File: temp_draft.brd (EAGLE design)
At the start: 76.7 x 34.5 mm, 39 parts, among them IC1 NCS21911SN2T1G, IC2 NCS21911SN2T1G, IC3 NCS21911SN2T1G, IC4 NCS21911SN2T1G

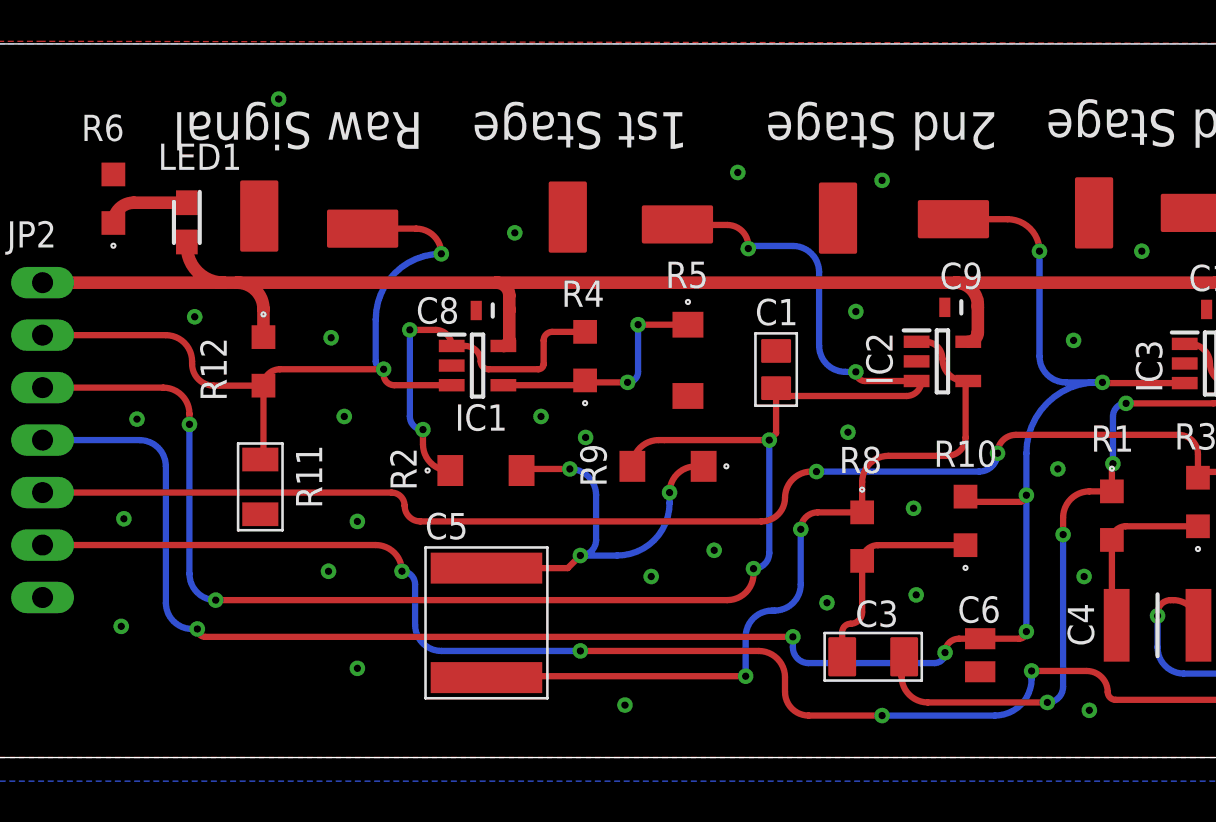
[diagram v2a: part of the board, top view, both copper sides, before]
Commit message: changed vias to GND vias
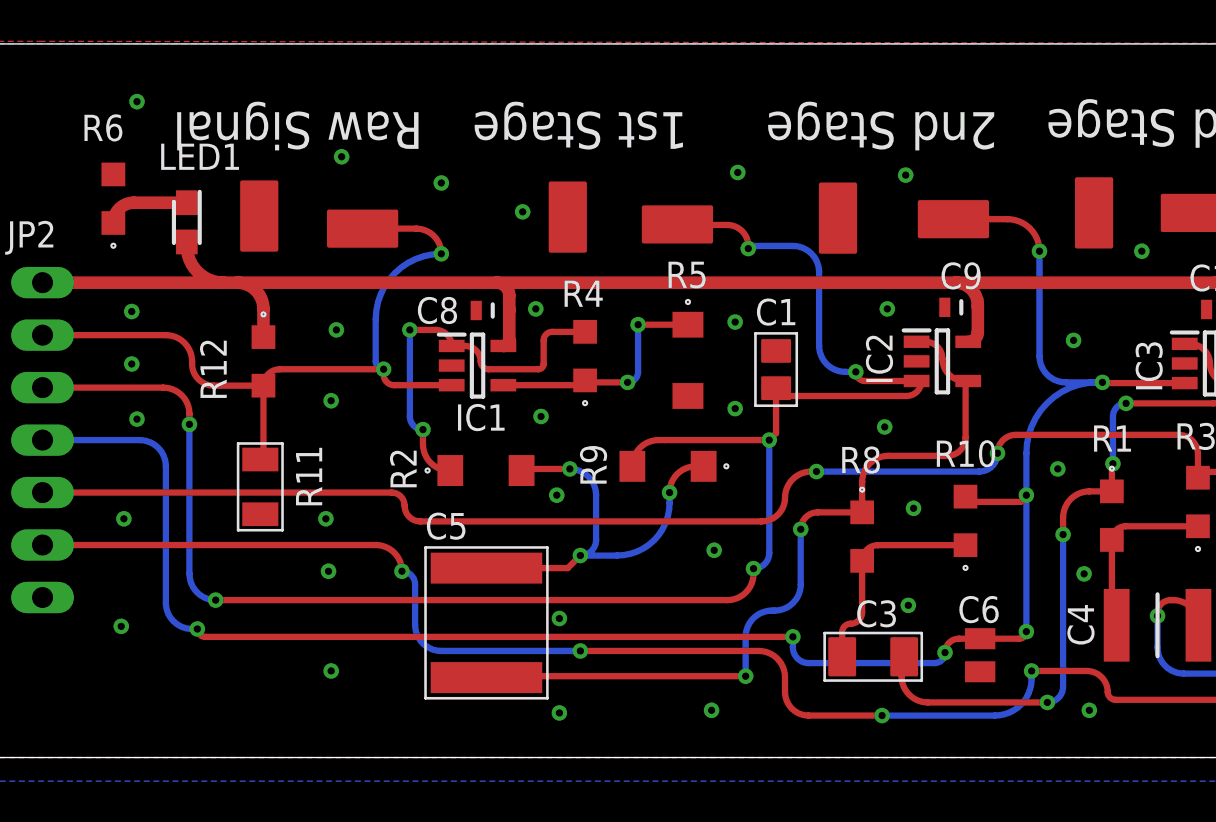
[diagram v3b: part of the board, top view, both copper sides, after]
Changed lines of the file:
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@@
 <drawing>
 <settings>
-<setting alwaysvectorfont="yes"/>
+<setting alwaysvectorfont="no"/>
 <setting verticaltext="up"/>
 </settings>
@@
 <vertex x="76.454" y="34.544"/>
 </polygon>
-<via x="13.97" y="31.877" extent="1-16" drill="0.35"/>
+<via x="7.112" y="31.75" extent="1-16" drill="0.35"/>
 <contactref element="R6" pad="2"/>
-<wire x1="67.272" y1="21.463" x2="65.2018" y2="26.4922" width="0" layer="19" extent="1-1"/>
-<wire x1="66.0854" y1="18.8976" x2="67.272" y2="21.463" width="0" layer="19" extent="1-1"/>
-<wire x1="58.89" y1="21.6916" x2="66.0854" y2="18.8976" width="0" layer="19" extent="1-1"/>
-<wire x1="57.8304" y1="19.0754" x2="58.89" y2="21.6916" width="0" layer="19" extent="1-1"/>
-<wire x1="53.4416" y1="26.3652" x2="58.89" y2="21.6916" width="0" layer="19" extent="1-1"/>
-<wire x1="65.7352" y1="11.0716" x2="66.0854" y2="18.8976" width="0" layer="19" extent="1-1"/>
-<wire x1="62.23" y1="11.066" x2="65.7352" y2="11.0716" width="0" layer="19" extent="1-1"/>
-<wire x1="46.2154" y1="21.7932" x2="53.4416" y2="26.3652" width="0" layer="19" extent="1-1"/>
-<wire x1="44.851" y1="19.177" x2="46.2154" y2="21.7932" width="0" layer="19" extent="1-1"/>
-<wire x1="41.0464" y1="26.1112" x2="46.2154" y2="21.7932" width="0" layer="19" extent="1-1"/>
-<wire x1="38.0492" y1="19.6816" x2="44.851" y2="19.177" width="0" layer="19" extent="1-1"/>
-<wire x1="33.782" y1="17.5028" x2="38.0492" y2="19.6816" width="0" layer="19" extent="1-1"/>
-<wire x1="27.9654" y1="26.162" x2="33.782" y2="17.5028" width="0" layer="19" extent="1-1"/>
-<wire x1="23.5332" y1="21.6408" x2="27.9654" y2="26.162" width="0" layer="19" extent="1-1"/>
-<wire x1="22.3466" y1="18.9738" x2="23.5332" y2="21.6408" width="0" layer="19" extent="1-1"/>
-<wire x1="13.0302" y1="26.2128" x2="23.5332" y2="21.6408" width="0" layer="19" extent="1-1"/>
-<wire x1="13.97" y1="31.877" x2="13.0302" y2="26.2128" width="0" layer="19" extent="1-1"/>
-<wire x1="13.081" y1="11.7772" x2="22.3466" y2="18.9738" width="0" layer="19" extent="1-1"/>
-<wire x1="2.54" y1="7.747" x2="13.081" y2="11.7772" width="0" layer="19" extent="1-1"/>
-<wire x1="5.969" y1="28.226" x2="2.54" y2="7.747" width="0" layer="19" extent="1-1"/>
-<wire x1="47.9298" y1="4.153" x2="44.851" y2="19.177" width="0" layer="19" extent="1-1"/>
+<via x="16.764" y="20.701" extent="1-16" drill="0.35"/>
+<via x="21.844" y="27.813" extent="1-16" drill="0.35"/>
+<via x="17.018" y="29.083" extent="1-16" drill="0.35"/>
+<via x="16.256" y="11.557" extent="1-16" drill="0.35"/>
+<via x="16.383" y="9.017" extent="1-16" drill="0.35"/>
+<via x="6.35" y="6.35" extent="1-16" drill="0.35"/>
+<via x="36.195" y="28.321" extent="1-16" drill="0.35"/>
+<via x="74.168" y="26.289" extent="1-16" drill="0.35"/>
+<via x="74.041" y="21.209" extent="1-16" drill="0.35"/>
+<via x="73.406" y="15.494" extent="1-16" drill="0.35"/>
+<via x="71.628" y="10.541" extent="1-16" drill="0.35"/>
+<via x="71.12" y="4.826" extent="1-16" drill="0.35"/>
+<via x="53.213" y="2.286" extent="1-16" drill="0.35"/>
+<via x="34.925" y="2.286" extent="1-16" drill="0.35"/>
+<via x="27.559" y="2.159" extent="1-16" drill="0.35"/>
+<via x="16.51" y="4.191" extent="1-16" drill="0.35"/>
+<via x="43.434" y="21.717" extent="1-16" drill="0.35"/>
+<via x="36.068" y="21.082" extent="1-16" drill="0.35"/>
+<via x="62.865" y="27.051" extent="1-16" drill="0.35"/>
+<via x="64.643" y="21.463" extent="1-16" drill="0.35"/>
+<via x="65.024" y="4.572" extent="1-16" drill="0.35"/>
+<via x="35.052" y="10.033" extent="1-16" drill="0.35"/>
+<via x="6.858" y="19.05" extent="1-16" drill="0.35"/>
+<via x="6.858" y="21.59" extent="1-16" drill="0.35"/>
+<via x="16.51" y="17.272" extent="1-16" drill="0.35"/>
+<via x="7.112" y="16.383" extent="1-16" drill="0.35"/>
+<via x="6.477" y="11.557" extent="1-16" drill="0.35"/>
+<via x="27.559" y="6.731" extent="1-16" drill="0.35"/>
+<via x="36.068" y="16.891" extent="1-16" drill="0.35"/>
+<via x="25.781" y="26.416" extent="1-16" drill="0.35"/>
+<via x="44.323" y="28.194" extent="1-16" drill="0.35"/>
+<via x="55.753" y="24.511" extent="1-16" drill="0.35"/>
+<via x="52.451" y="20.193" extent="1-16" drill="0.35"/>
+<via x="51.689" y="13.97" extent="1-16" drill="0.35"/>
+<via x="52.959" y="8.89" extent="1-16" drill="0.35"/>
+<via x="64.008" y="16.129" extent="1-16" drill="0.35"/>
+<via x="26.416" y="21.717" extent="1-16" drill="0.35"/>
+<via x="26.67" y="16.51" extent="1-16" drill="0.35"/>
+<via x="27.432" y="12.7" extent="1-16" drill="0.35"/>
+<via x="44.45" y="7.366" extent="1-16" drill="0.35"/>
+<via x="44.704" y="12.065" extent="1-16" drill="0.35"/>
+<via x="43.307" y="16.002" extent="1-16" drill="0.35"/>
+<via x="64.008" y="9.525" extent="1-16" drill="0.35"/>
 </signal>
 <signal name="N$1">
@@
 <wire x1="25.1332" y1="22.3648" x2="24.511" y2="22.987" width="0.6096" layer="1" curve="90"/>
 </signal>
-<signal name="GND1">
-<via x="9.906" y="21.336" extent="1-16" drill="0.35"/>
-</signal>
-<signal name="GND2">
-<via x="6.35" y="6.35" extent="1-16" drill="0.35"/>
-</signal>
-<signal name="GND3">
-<via x="16.51" y="20.32" extent="1-16" drill="0.35"/>
-</signal>
-<signal name="GND4">
-<via x="17.78" y="11.43" extent="1-16" drill="0.35"/>
-</signal>
-<signal name="GND5">
-<via x="17.78" y="4.318" extent="1-16" drill="0.35"/>
-</signal>
-<signal name="GND6">
-<via x="25.4" y="25.4" extent="1-16" drill="0.35"/>
-</signal>
-<signal name="GND7">
-<via x="26.67" y="16.51" extent="1-16" drill="0.35"/>
-</signal>
-<signal name="GND8">
-<via x="32.004" y="8.763" extent="1-16" drill="0.35"/>
-</signal>
-<signal name="GND9">
-<via x="30.734" y="2.54" extent="1-16" drill="0.35"/>
-</signal>
-<signal name="GND10">
-<via x="43.18" y="27.94" extent="1-16" drill="0.35"/>
-</signal>
-<signal name="GND11">
-<via x="41.91" y="21.59" extent="1-16" drill="0.35"/>
-</signal>
-<signal name="GND12">
-<via x="41.529" y="15.748" extent="1-16" drill="0.35"/>
-</signal>
-<signal name="GND13">
-<via x="40.513" y="7.493" extent="1-16" drill="0.35"/>
-</signal>
-<signal name="GND14">
-<via x="52.451" y="20.193" extent="1-16" drill="0.35"/>
-</signal>
-<signal name="GND15">
-<via x="51.689" y="13.97" extent="1-16" drill="0.35"/>
-</signal>
-<signal name="GND16">
-<via x="52.959" y="8.763" extent="1-16" drill="0.35"/>
-</signal>
-<signal name="GND17">
-<via x="62.865" y="27.051" extent="1-16" drill="0.35"/>
-</signal>
-<signal name="GND18">
-<via x="64.643" y="21.463" extent="1-16" drill="0.35"/>
-</signal>
-<signal name="GND19">
-<via x="64.008" y="16.129" extent="1-16" drill="0.35"/>
-</signal>
-<signal name="GND20">
-<via x="65.024" y="4.572" extent="1-16" drill="0.35"/>
-</signal>
-<signal name="GND21">
-<via x="7.112" y="16.383" extent="1-16" drill="0.35"/>
-</signal>
-<signal name="GND22">
-<via x="64.008" y="9.525" extent="1-16" drill="0.35"/>
-</signal>
-<signal name="N$2">
-<via x="6.477" y="11.557" extent="1-16" drill="0.35"/>
-</signal>
-<signal name="N$3">
-<via x="17.145" y="16.51" extent="1-16" drill="0.35"/>
-</signal>
-<signal name="N$4">
-<via x="16.383" y="9.017" extent="1-16" drill="0.35"/>
-</signal>
-<signal name="N$8">
-<via x="28.829" y="15.494" extent="1-16" drill="0.35"/>
-</signal>
-<signal name="N$9">
-<via x="35.052" y="10.033" extent="1-16" drill="0.35"/>
-</signal>
-<signal name="N$10">
-<via x="44.831" y="7.874" extent="1-16" drill="0.35"/>
-</signal>
-<signal name="N$11">
-<via x="44.704" y="12.065" extent="1-16" drill="0.35"/>
-</signal>
-<signal name="N$12">
-<via x="55.753" y="24.511" extent="1-16" drill="0.35"/>
-</signal>
-<signal name="N$13">
-<via x="53.213" y="2.286" extent="1-16" drill="0.35"/>
-</signal>
-<signal name="N$14">
-<via x="74.168" y="26.289" extent="1-16" drill="0.35"/>
-</signal>
-<signal name="N$15">
-<via x="74.041" y="21.209" extent="1-16" drill="0.35"/>
-</signal>
-<signal name="N$16">
-<via x="73.406" y="15.494" extent="1-16" drill="0.35"/>
-</signal>
-<signal name="N$17">
-<via x="71.628" y="10.541" extent="1-16" drill="0.35"/>
-</signal>
-<signal name="N$18">
-<via x="71.12" y="4.826" extent="1-16" drill="0.35"/>
-</signal>
-<signal name="N$19">
-<via x="36.195" y="28.321" extent="1-16" drill="0.35"/>
-</signal>
 <signal name="N$20">

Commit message: updated labels
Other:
- board size 76.7 x 34.5 mm -> 82.2 x 34.5 mm
- board text added: "BAJA SAE ELECTRICALS DESIGNED BY RYAN THAI PCB TEMPERATURE SENSOR YEAR OF 2021-2022"
- board text added: "GND"
- board text added: "INPUT1"
- board text added: "OUTPUT1"
- board text added: "OUTPUT2"
- board text added: "OUTPUT3"
- board text added: "OUTPUT4"
- board text added: "V_12V"
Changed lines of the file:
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@@
 <drawing>
 <settings>
-<setting alwaysvectorfont="no"/>
+<setting alwaysvectorfont="yes"/>
 <setting verticaltext="up"/>
 </settings>
@@
 <board>
 <plain>
-<wire x1="0" y1="0" x2="76.708" y2="0" width="0" layer="20"/>
+<wire x1="-5.461" y1="0" x2="76.708" y2="0" width="0" layer="20"/>
 <wire x1="76.708" y1="0" x2="76.454" y2="34.544" width="0" layer="20"/>
-<wire x1="76.454" y1="34.544" x2="0" y2="34.544" width="0" layer="20"/>
-<wire x1="0" y1="34.544" x2="0" y2="0" width="0" layer="20"/>
+<wire x1="76.454" y1="34.544" x2="-5.461" y2="34.544" width="0" layer="20"/>
+<wire x1="-5.461" y1="34.544" x2="-5.461" y2="0" width="0" layer="20"/>
 <text x="48.768" y="31.242" size="1.778" layer="21" rot="SR180">2nd Stage</text>
 <text x="33.782" y="31.242" size="1.778" layer="21" rot="SR180">1st Stage</text>
@@
 <text x="74.549" y="31.242" size="1.778" layer="21" rot="SR180">4th Stage</text>
 <text x="20.955" y="31.242" size="1.778" layer="21" rot="SR180">Raw Signal</text>
+<text x="-3.048" y="22.733" size="0.6096" layer="25">V_12V</text>
+<text x="-3.175" y="20.193" size="0.6096" layer="25">INPUT1</text>
+<text x="-3.302" y="17.526" size="0.6096" layer="25">OUTPUT1</text>
+<text x="-3.429" y="14.986" size="0.6096" layer="25">OUTPUT2</text>
+<text x="-3.302" y="12.446" size="0.6096" layer="25">OUTPUT3</text>
+<text x="-3.429" y="9.906" size="0.6096" layer="25">OUTPUT4</text>
+<text x="-3.302" y="7.366" size="0.6096" layer="25">GND</text>
+<text x="75.311" y="29.464" size="0.6096" layer="26" rot="MR0">BAJA SAE ELECTRICALS
+DESIGNED BY RYAN THAI
+PCB TEMPERATURE SENSOR
+YEAR OF 2021-2022</text>
 </plain>
 <attributes>
@@
 <element name="TP10" library="SamacSys_Parts" package="1.85X3.45_MM" value="" x="64.262" y="28.194" smashed="yes" rot="R180"/>
 <element name="JP2" library="pinhead" library_urn="urn:adsk.eagle:library:325" package="1X07" package3d_urn="urn:adsk.eagle:package:22477/2" value="" x="2.54" y="15.367" smashed="yes" rot="MR270">
-<attribute name="NAME" x="0.8128" y="24.6888" size="1.27" layer="25" ratio="10"/>
+<attribute name="NAME" x="0.9398" y="24.6888" size="1.27" layer="25" ratio="10"/>
 <attribute name="POPULARITY" value="0" x="2.54" y="15.367" size="1.778" layer="28" rot="MR270" display="off"/>
 <attribute name="VALUE" x="5.715" y="24.257" size="1.27" layer="28" rot="MR270"/>
@@
 <contactref element="JP2" pad="7"/>
 <polygon width="0.3048" layer="1">
-<vertex x="0" y="34.671"/>
-<vertex x="0" y="0"/>
+<vertex x="-5.461" y="34.671"/>
+<vertex x="-5.461" y="0"/>
 <vertex x="76.581" y="0"/>
 <vertex x="76.581" y="34.544"/>
@@
 </polygon>
 <polygon width="0.3048" layer="16">
-<vertex x="0" y="34.544"/>
-<vertex x="0" y="-1.143"/>
+<vertex x="-5.461" y="34.544"/>
+<vertex x="-5.461" y="-1.143"/>
 <vertex x="76.454" y="-1.143"/>
 <vertex x="76.454" y="34.544"/>
@@
 </drawing>
 <compatibility>
+<note version="6.3" minversion="6.2.2" severity="warning">
+Since Version 6.2.2 text objects can contain more than one line,
+which will not be processed correctly with this version.
+</note>
 <note version="8.2" severity="warning">
 Since Version 8.2, EAGLE supports online libraries. The ids
